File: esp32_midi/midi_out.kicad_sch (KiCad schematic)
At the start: 3 parts

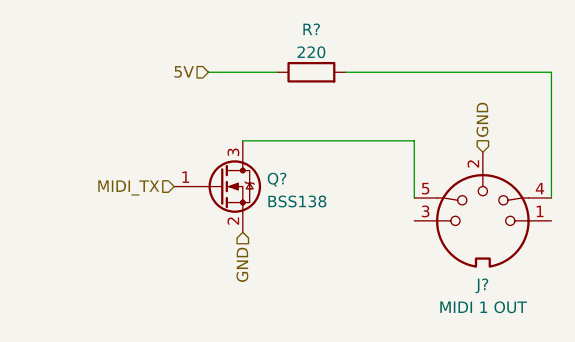
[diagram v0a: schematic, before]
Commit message: work in progress, added usb-c flasher, add display connector, add midi connections
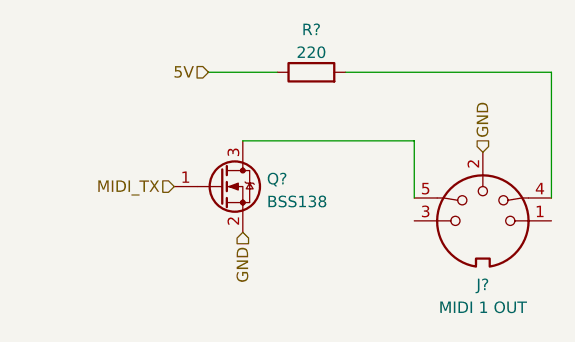
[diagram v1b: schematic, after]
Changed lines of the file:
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@@
-(kicad_sch (version 20211123) (generator eeschema)
+(kicad_sch (version 20230121) (generator eeschema)
   (paper "A4")
   (wire (pts (xy 99.06 50.8) (xy 121.92 50.8))
-    (stroke (width 0) (type default) (color 0 0 0 0))
+    (stroke (width 0) (type default))
   )
   (wire (pts (xy 121.92 50.8) (xy 121.92 64.77))
-    (stroke (width 0) (type default) (color 0 0 0 0))
+    (stroke (width 0) (type default))
   )
   (wire (pts (xy 83.82 50.8) (xy 91.44 50.8))
-    (stroke (width 0) (type default) (color 0 0 0 0))
+    (stroke (width 0) (type default))
   )
   (wire (pts (xy 87.63 58.42) (xy 106.68 58.42))
-    (stroke (width 0) (type default) (color 0 0 0 0))
+    (stroke (width 0) (type default))
   )
   (wire (pts (xy 106.68 58.42) (xy 106.68 64.77))
-    (stroke (width 0) (type default) (color 0 0 0 0))
+    (stroke (width 0) (type default))
   )
-  (hierarchical_label "5V" (shape input) (at 83.82 50.8 180)
+  (hierarchical_label "5V" (shape input) (at 83.82 50.8 180) (fields_autoplaced)
     (effects (font (size 1.27 1.27)) (justify right))
   )
-  (hierarchical_label "MIDI_TX" (shape input) (at 80.01 63.5 180)
+  (hierarchical_label "MIDI_TX" (shape input) (at 80.01 63.5 180) (fields_autoplaced)
     (effects (font (size 1.27 1.27)) (justify right))
   )
-  (hierarchical_label "GND" (shape input) (at 114.3 59.69 90)
+  (hierarchical_label "GND" (shape input) (at 114.3 59.69 90) (fields_autoplaced)
     (effects (font (size 1.27 1.27)) (justify left))
   )
-  (hierarchical_label "GND" (shape input) (at 87.63 68.58 270)
+  (hierarchical_label "GND" (shape input) (at 87.63 68.58 270) (fields_autoplaced)
     (effects (font (size 1.27 1.27)) (justify right))
   )
   (symbol (lib_id "Connector:DIN-5_180degree") (at 114.3 67.31 0) (mirror y) (unit 1)
-    (in_bom yes) (on_board yes) (fields_autoplaced)
-    (property "Reference" "J?" (id 0) (at 114.2999 74.4204 0))
-    (property "Value" "MIDI 1 OUT" (id 1) (at 114.2999 76.9573 0))
-    (property "Footprint" "" (id 2) (at 114.3 67.31 0)
+    (in_bom yes) (on_board yes) (dnp no) (fields_autoplaced)
+    (property "Reference" "J?" (at 114.2999 74.4204 0)
+      (effects (font (size 1.27 1.27)))
+    )
+    (property "Value" "MIDI 1 OUT" (at 114.2999 76.9573 0)
+      (effects (font (size 1.27 1.27)))
+    )
+    (property "Footprint" "" (at 114.3 67.31 0)
       (effects (font (size 1.27 1.27)) hide)
     )
-    (property "Datasheet" "http://www.mouser.com/ds/2/18/40_c091_abd_e-75918.pdf" (id 3) (at 114.3 67.31 0)
+    (property "Datasheet" "http://www.mouser.com/ds/2/18/40_c091_abd_e-75918.pdf" (at 114.3 67.31 0)
       (effects (font (size 1.27 1.27)) hide)
     )
@@
     (pin "4")
     (pin "5")
+    (instances
+      (project "esp32_midi"
+        (path "/e33c0603-5c0d-4712-ab63-5756d1504b4c/6690eb41-2c1d-4abf-90f8-fc4c3740650e/23ac7157-3583-490b-a889-9bba9a4271ea"
+          (reference "J?") (unit 1)
+        )
+        (path "/e33c0603-5c0d-4712-ab63-5756d1504b4c/6690eb41-2c1d-4abf-90f8-fc4c3740650e/067e608b-1500-4656-956d-29b5641ffb6f"
+          (reference "J?") (unit 1)
+        )
+      )
+    )
   )
   (symbol (lib_id "Transistor_FET:BSS138") (at 85.09 63.5 0) (unit 1)
-    (in_bom yes) (on_board yes) (fields_autoplaced)
-    (property "Reference" "Q?" (id 0) (at 90.297 62.6653 0)
+    (in_bom yes) (on_board yes) (dnp no) (fields_autoplaced)
+    (property "Reference" "Q?" (at 90.297 62.6653 0)
       (effects (font (size 1.27 1.27)) (justify left))
     )
-    (property "Value" "BSS138" (id 1) (at 90.297 65.2022 0)
+    (property "Value" "BSS138" (at 90.297 65.2022 0)
       (effects (font (size 1.27 1.27)) (justify left))
     )
-    (property "Footprint" "Package_TO_SOT_SMD:SOT-23" (id 2) (at 90.17 65.405 0)
+    (property "Footprint" "Package_TO_SOT_SMD:SOT-23" (at 90.17 65.405 0)
       (effects (font (size 1.27 1.27) italic) (justify left) hide)
     )
-    (property "Datasheet" "https://www.onsemi.com/pub/Collateral/BSS138-D.PDF" (id 3) (at 85.09 63.5 0)
+    (property "Datasheet" "https://www.onsemi.com/pub/Collateral/BSS138-D.PDF" (at 85.09 63.5 0)
       (effects (font (size 1.27 1.27)) (justify left) hide)
     )
@@
     (pin "2")
     (pin "3")
+    (instances
+      (project "esp32_midi"
+        (path "/e33c0603-5c0d-4712-ab63-5756d1504b4c/6690eb41-2c1d-4abf-90f8-fc4c3740650e/23ac7157-3583-490b-a889-9bba9a4271ea"
+          (reference "Q?") (unit 1)
+        )
+        (path "/e33c0603-5c0d-4712-ab63-5756d1504b4c/6690eb41-2c1d-4abf-90f8-fc4c3740650e/067e608b-1500-4656-956d-29b5641ffb6f"
+          (reference "Q?") (unit 1)
+        )
+      )
+    )
   )
   (symbol (lib_id "Device:R") (at 95.25 50.8 90) (unit 1)
-    (in_bom yes) (on_board yes) (fields_autoplaced)
-    (property "Reference" "R?" (id 0) (at 95.25 46.0842 90))
-    (property "Value" "220" (id 1) (at 95.25 48.6211 90))
-    (property "Footprint" "" (id 2) (at 95.25 52.578 90)
+    (in_bom yes) (on_board yes) (dnp no) (fields_autoplaced)
+    (property "Reference" "R?" (at 95.25 46.0842 90)
+      (effects (font (size 1.27 1.27)))
+    )
+    (property "Value" "220" (at 95.25 48.6211 90)
+      (effects (font (size 1.27 1.27)))
+    )
+    (property "Footprint" "" (at 95.25 52.578 90)
       (effects (font (size 1.27 1.27)) hide)
     )
-    (property "Datasheet" "~" (id 3) (at 95.25 50.8 0)
+    (property "Datasheet" "~" (at 95.25 50.8 0)
       (effects (font (size 1.27 1.27)) hide)
     )
     (pin "1")
     (pin "2")
+    (instances
+      (project "esp32_midi"
+        (path "/e33c0603-5c0d-4712-ab63-5756d1504b4c/6690eb41-2c1d-4abf-90f8-fc4c3740650e/23ac7157-3583-490b-a889-9bba9a4271ea"
+          (reference "R?") (unit 1)
+        )
+        (path "/e33c0603-5c0d-4712-ab63-5756d1504b4c/6690eb41-2c1d-4abf-90f8-fc4c3740650e/067e608b-1500-4656-956d-29b5641ffb6f"
+          (reference "R?") (unit 1)
+        )
+      )
+    )
   )
 )

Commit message: More footprints applied
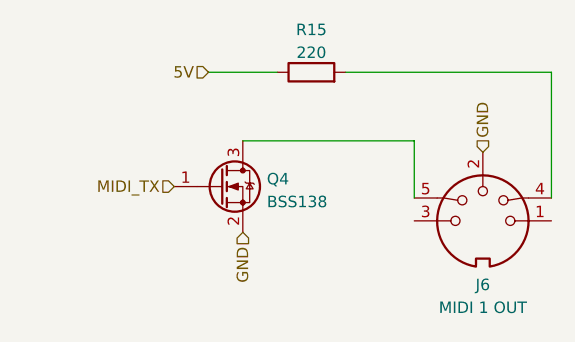
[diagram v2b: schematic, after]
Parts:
- J6: renamed from J?; footprint (none) -> ordentliche-teile:scheißmidi
- R15: renamed from R?; footprint (none) -> Resistor_SMD:R_0402_1005Metric
- gave numbers to parts that had none: 1
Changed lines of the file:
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@@
   (symbol (lib_id "Connector:DIN-5_180degree") (at 114.3 67.31 0) (mirror y) (unit 1)
     (in_bom yes) (on_board yes) (dnp no) (fields_autoplaced)
-    (property "Reference" "J?" (at 114.2999 74.4204 0)
+    (property "Reference" "J6" (at 114.2999 74.4204 0)
       (effects (font (size 1.27 1.27)))
     )
@@
       (effects (font (size 1.27 1.27)))
     )
-    (property "Footprint" "" (at 114.3 67.31 0)
+    (property "Footprint" "ordentliche-teile:scheißmidi" (at 114.3 67.31 0)
       (effects (font (size 1.27 1.27)) hide)
     )
@@
       (project "esp32_midi"
         (path "/e33c0603-5c0d-4712-ab63-5756d1504b4c/6690eb41-2c1d-4abf-90f8-fc4c3740650e/23ac7157-3583-490b-a889-9bba9a4271ea"
-          (reference "J?") (unit 1)
+          (reference "J6") (unit 1)
         )
         (path "/e33c0603-5c0d-4712-ab63-5756d1504b4c/6690eb41-2c1d-4abf-90f8-fc4c3740650e/067e608b-1500-4656-956d-29b5641ffb6f"
-          (reference "J?") (unit 1)
+          (reference "J4") (unit 1)
         )
       )
@@
   (symbol (lib_id "Transistor_FET:BSS138") (at 85.09 63.5 0) (unit 1)
     (in_bom yes) (on_board yes) (dnp no) (fields_autoplaced)
-    (property "Reference" "Q?" (at 90.297 62.6653 0)
+    (property "Reference" "Q4" (at 90.297 62.6653 0)
       (effects (font (size 1.27 1.27)) (justify left))
     )
@@
       (project "esp32_midi"
         (path "/e33c0603-5c0d-4712-ab63-5756d1504b4c/6690eb41-2c1d-4abf-90f8-fc4c3740650e/23ac7157-3583-490b-a889-9bba9a4271ea"
-          (reference "Q?") (unit 1)
+          (reference "Q4") (unit 1)
         )
         (path "/e33c0603-5c0d-4712-ab63-5756d1504b4c/6690eb41-2c1d-4abf-90f8-fc4c3740650e/067e608b-1500-4656-956d-29b5641ffb6f"
-          (reference "Q?") (unit 1)
+          (reference "Q1") (unit 1)
         )
       )
@@
   (symbol (lib_id "Device:R") (at 95.25 50.8 90) (unit 1)
     (in_bom yes) (on_board yes) (dnp no) (fields_autoplaced)
-    (property "Reference" "R?" (at 95.25 46.0842 90)
+    (property "Reference" "R15" (at 95.25 46.0842 90)
       (effects (font (size 1.27 1.27)))
     )
@@
       (effects (font (size 1.27 1.27)))
     )
-    (property "Footprint" "" (at 95.25 52.578 90)
+    (property "Footprint" "Resistor_SMD:R_0402_1005Metric" (at 95.25 52.578 90)
       (effects (font (size 1.27 1.27)) hide)
     )
@@
       (project "esp32_midi"
         (path "/e33c0603-5c0d-4712-ab63-5756d1504b4c/6690eb41-2c1d-4abf-90f8-fc4c3740650e/23ac7157-3583-490b-a889-9bba9a4271ea"
-          (reference "R?") (unit 1)
+          (reference "R15") (unit 1)
         )
         (path "/e33c0603-5c0d-4712-ab63-5756d1504b4c/6690eb41-2c1d-4abf-90f8-fc4c3740650e/067e608b-1500-4656-956d-29b5641ffb6f"
-          (reference "R?") (unit 1)
+          (reference "R2") (unit 1)
         )
       )

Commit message: Started work on PCB
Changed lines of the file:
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@@
   (symbol (lib_id "Connector:DIN-5_180degree") (at 114.3 67.31 0) (mirror y) (unit 1)
     (in_bom yes) (on_board yes) (dnp no) (fields_autoplaced)
-    (property "Reference" "J6" (at 114.2999 74.4204 0)
+    (property "Reference" "J6" (at 114.2999 74.93 0)
       (effects (font (size 1.27 1.27)))
     )
-    (property "Value" "MIDI 1 OUT" (at 114.2999 76.9573 0)
+    (property "Value" "MIDI 1 OUT" (at 114.2999 77.47 0)
       (effects (font (size 1.27 1.27)))
     )

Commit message: More pcb
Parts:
- R15: footprint Resistor_SMD:R_0402_1005Metric -> Resistor_SMD:R_1206_3216Metric
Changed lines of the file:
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@@
       (effects (font (size 1.27 1.27)))
     )
-    (property "Footprint" "Resistor_SMD:R_0402_1005Metric" (at 95.25 52.578 90)
+    (property "Footprint" "Resistor_SMD:R_1206_3216Metric" (at 95.25 52.578 90)
       (effects (font (size 1.27 1.27)) hide)
     )

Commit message: Everything changed
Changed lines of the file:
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@@
-(kicad_sch (version 20230121) (generator eeschema)
+(kicad_sch (version 20230620) (generator eeschema)
   (paper "A4")
   (wire (pts (xy 99.06 50.8) (xy 121.92 50.8))
@@
   )
   (wire (pts (xy 83.82 50.8) (xy 91.44 50.8))
+    (stroke (width 0) (type default))
+  )
+  (wire (pts (xy 73.66 63.5) (xy 80.01 63.5))
     (stroke (width 0) (type default))
   )
@@
     (effects (font (size 1.27 1.27)) (justify right))
   )
-  (hierarchical_label "MIDI_TX" (shape input) (at 80.01 63.5 180) (fields_autoplaced)
+  (hierarchical_label "MIDI_TX" (shape input) (at 73.66 63.5 180) (fields_autoplaced)
     (effects (font (size 1.27 1.27)) (justify right))
   )
@@
     )
     (property "Datasheet" "http://www.mouser.com/ds/2/18/40_c091_abd_e-75918.pdf" (at 114.3 67.31 0)
+      (effects (font (size 1.27 1.27)) hide)
+    )
+    (property "Description" "" (at 114.3 67.31 0)
       (effects (font (size 1.27 1.27)) hide)
     )
@@
       (effects (font (size 1.27 1.27)) (justify left) hide)
     )
+    (property "Description" "" (at 85.09 63.5 0)
+      (effects (font (size 1.27 1.27)) hide)
+    )
     (pin "1")
     (pin "2")
@@
       (effects (font (size 1.27 1.27)) hide)
     )
+    (property "Description" "" (at 95.25 50.8 0)
+      (effects (font (size 1.27 1.27)) hide)
+    )

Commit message: First load of bug fixes
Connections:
- no-connect marks 0 -> 2
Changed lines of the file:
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@@
 (kicad_sch (version 20230620) (generator eeschema)
   (paper "A4")
+  (no_connect (at 121.92 67.31))
+  (no_connect (at 106.68 67.31))
   (wire (pts (xy 99.06 50.8) (xy 121.92 50.8))
     (stroke (width 0) (type default))
@@
       (effects (font (size 1.27 1.27)) hide)
     )
-    (property "Description" "" (at 114.3 67.31 0)
+    (property "Description" "5-pin DIN connector (5-pin DIN-5 stereo)" (at 114.3 67.31 0)
       (effects (font (size 1.27 1.27)) hide)
     )
@@
       (effects (font (size 1.27 1.27)) (justify left) hide)
     )
-    (property "Description" "" (at 85.09 63.5 0)
+    (property "Description" "50V Vds, 0.22A Id, N-Channel MOSFET, SOT-23" (at 85.09 63.5 0)
       (effects (font (size 1.27 1.27)) hide)
     )
@@
       (effects (font (size 1.27 1.27)) hide)
     )
-    (property "Description" "" (at 95.25 50.8 0)
+    (property "Description" "Resistor" (at 95.25 50.8 0)
       (effects (font (size 1.27 1.27)) hide)
     )

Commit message: Update parts numbers
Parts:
- J6, Q4, R15: Field-1 (none) -> ${DNP}
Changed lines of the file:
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@@
+      (effects (font (size 1.27 1.27)) hide)
+    )
+    (property "Field-1" "${DNP}" (at 114.3 67.31 0)
+      (effects (font (size 1.27 1.27)) hide)
+    )
+    (property "Field-1" "${DNP}" (at 114.3 67.31 0)
       (effects (font (size 1.27 1.27)) hide)
     )
@@
       (effects (font (size 1.27 1.27)) hide)
     )
+    (property "Field-1" "${DNP}" (at 85.09 63.5 0)
+      (effects (font (size 1.27 1.27)) hide)
+    )
+    (property "Field-1" "${DNP}" (at 85.09 63.5 0)
+      (effects (font (size 1.27 1.27)) hide)
+    )
     (pin "1")
     (pin "2")
@@
       (effects (font (size 1.27 1.27)) hide)
     )
+    (property "Field-1" "${DNP}" (at 95.25 50.8 0)
+      (effects (font (size 1.27 1.27)) hide)
+    )
+    (property "Field-1" "${DNP}" (at 95.25 50.8 0)
+      (effects (font (size 1.27 1.27)) hide)
+    )
